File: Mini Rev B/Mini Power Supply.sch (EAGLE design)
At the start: 20 parts, among them J1 POWER_JACKPTH

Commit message: Changed the input to a JST and connected the ON LED to VCC
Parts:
- removed IADJ_SEL: (no value), pinhead:PINHD-1X2
- removed J1: POWER_JACKPTH, SparkFun-Connectors:POWER_JACKPTH
- added INPUT: M02JST-PTH-2, SparkFun-Connectors:M02JST-PTH-2
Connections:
- removed net N$4: IADJ.ADJ, IADJ_SEL.1, R3.CW, R6.1
- net GND: now also INPUT.1; no longer J1.GND, J1.GNDBREAK
- net VADJ_IN: now also IADJ.ADJ, R3.CW, R6.1; no longer IADJ_SEL.2
- net VCC: now also INPUT.2, ON.A; no longer J1.PWR
- net VOUT: no longer ON.A
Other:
- note removed: "Change the input to a JST"
- note removed: "This should be connected to VCC"
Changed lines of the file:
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@@
 <part name="R5" library="rcl" deviceset="R-EU_" device="R0805" value="100Ω"/>
 <part name="R6" library="rcl" deviceset="R-EU_" device="R0805" value="100Ω"/>
-<part name="IADJ_SEL" library="pinhead" deviceset="PINHD-1X2" device=""/>
 <part name="ON" library="led" deviceset="LED" device="CHIPLED_1206"/>
 <part name="R7" library="rcl" deviceset="R-EU_" device="R0805" value="1kΩ"/>
 <part name="GND4" library="supply1" deviceset="GND" device=""/>
 <part name="I_PRB" library="pinhead" deviceset="PINHD-1X2" device=""/>
-<part name="J1" library="SparkFun-Connectors" deviceset="POWER_JACK" device="PTH"/>
 <part name="GND6" library="supply1" deviceset="GND" device=""/>
 <part name="P+1" library="supply1" deviceset="VCC" device=""/>
 <part name="OUTPUT" library="SparkFun-Connectors" deviceset="M02" device="JST-PTH-2"/>
 <part name="SUPPLY10" library="supply2" deviceset="GND" device=""/>
+<part name="INPUT" library="SparkFun-Connectors" deviceset="M02" device="JST-PTH-2"/>
+<part name="P+3" library="supply1" deviceset="VCC" device=""/>
 </parts>
 <sheets>
 <sheet>
 <plain>
-<text x="-5.08" y="45.72" size="1.778" layer="91">Change the input
-to a JST</text>
-<text x="121.92" y="66.04" size="1.778" layer="91">This should be
-connected to VCC</text>
 <text x="76.2" y="88.9" size="1.778" layer="91">Add a current limiting
 indicator if possible</text>
@@
 <instance part="R5" gate="G$1" x="124.46" y="101.6" rot="R180"/>
 <instance part="R6" gate="G$1" x="137.16" y="101.6" rot="R180"/>
-<instance part="IADJ_SEL" gate="G$1" x="162.56" y="109.22"/>
 <instance part="ON" gate="G$1" x="134.62" y="50.8"/>
 <instance part="R7" gate="G$1" x="134.62" y="35.56" rot="R90"/>
 <instance part="GND4" gate="1" x="134.62" y="20.32"/>
 <instance part="I_PRB" gate="G$1" x="167.64" y="50.8"/>
-<instance part="J1" gate="G$1" x="12.7" y="27.94"/>
 <instance part="GND6" gate="1" x="20.32" y="17.78"/>
-<instance part="P+1" gate="VCC" x="25.4" y="50.8"/>
+<instance part="P+1" gate="VCC" x="20.32" y="50.8"/>
 <instance part="OUTPUT" gate="G$1" x="172.72" y="38.1" rot="R180"/>
 <instance part="SUPPLY10" gate="GND" x="162.56" y="25.4"/>
+<instance part="INPUT" gate="G$1" x="7.62" y="33.02"/>
+<instance part="P+3" gate="VCC" x="134.62" y="63.5"/>
 </instances>
 <busses>
@@
 </segment>
 <segment>
-<pinref part="ON" gate="G$1" pin="A"/>
-<wire x1="134.62" y1="53.34" x2="134.62" y2="60.96" width="0.1524" layer="91"/>
-<label x="132.08" y="60.96" size="1.778" layer="95"/>
-</segment>
-<segment>
 <pinref part="I_PRB" gate="G$1" pin="1"/>
 <wire x1="165.1" y1="53.34" x2="157.48" y2="53.34" width="0.1524" layer="91"/>
@@
 </segment>
 <segment>
-<pinref part="J1" gate="G$1" pin="PWR"/>
-<wire x1="15.24" y1="35.56" x2="25.4" y2="35.56" width="0.1524" layer="91"/>
+<wire x1="15.24" y1="35.56" x2="20.32" y2="35.56" width="0.1524" layer="91"/>
 <pinref part="P+1" gate="VCC" pin="VCC"/>
-<wire x1="25.4" y1="35.56" x2="25.4" y2="48.26" width="0.1524" layer="91"/>
+<wire x1="20.32" y1="35.56" x2="20.32" y2="48.26" width="0.1524" layer="91"/>
+<pinref part="INPUT" gate="G$1" pin="2"/>
+</segment>
+<segment>
+<pinref part="ON" gate="G$1" pin="A"/>
+<wire x1="134.62" y1="53.34" x2="134.62" y2="60.96" width="0.1524" layer="91"/>
+<pinref part="P+3" gate="VCC" pin="VCC"/>
 </segment>
 </net>
@@
 </segment>
 <segment>
-<pinref part="J1" gate="G$1" pin="GNDBREAK"/>
 <wire x1="15.24" y1="33.02" x2="20.32" y2="33.02" width="0.1524" layer="91"/>
-<wire x1="20.32" y1="33.02" x2="20.32" y2="30.48" width="0.1524" layer="91"/>
-<junction x="20.32" y="30.48"/>
-<wire x1="20.32" y1="30.48" x2="20.32" y2="20.32" width="0.1524" layer="91"/>
-<pinref part="J1" gate="G$1" pin="GND"/>
-<wire x1="15.24" y1="30.48" x2="20.32" y2="30.48" width="0.1524" layer="91"/>
+<wire x1="20.32" y1="33.02" x2="20.32" y2="20.32" width="0.1524" layer="91"/>
 <pinref part="GND6" gate="1" pin="GND"/>
+<pinref part="INPUT" gate="G$1" pin="1"/>
 </segment>
 <segment>
@@
 </segment>
 <segment>
-<pinref part="IADJ_SEL" gate="G$1" pin="2"/>
-<wire x1="160.02" y1="109.22" x2="152.4" y2="109.22" width="0.1524" layer="91"/>
-<wire x1="152.4" y1="109.22" x2="152.4" y2="88.9" width="0.1524" layer="91"/>
-<label x="147.32" y="86.36" size="1.778" layer="95"/>
+<label x="162.56" y="114.3" size="1.778" layer="95" rot="R180"/>
+<pinref part="IADJ" gate="1" pin="ADJ"/>
+<wire x1="88.9" y1="104.14" x2="88.9" y2="96.52" width="0.1524" layer="91"/>
+<pinref part="R3" gate="R?" pin="CW"/>
+<wire x1="129.54" y1="111.76" x2="147.32" y2="111.76" width="0.1524" layer="91"/>
+<pinref part="R6" gate="G$1" pin="1"/>
+<wire x1="142.24" y1="101.6" x2="147.32" y2="101.6" width="0.1524" layer="91"/>
+<wire x1="147.32" y1="101.6" x2="147.32" y2="111.76" width="0.1524" layer="91"/>
+<junction x="147.32" y="111.76"/>
+<wire x1="147.32" y1="111.76" x2="157.48" y2="111.76" width="0.1524" layer="91"/>
+<wire x1="88.9" y1="96.52" x2="147.32" y2="96.52" width="0.1524" layer="91"/>
+<wire x1="147.32" y1="96.52" x2="147.32" y2="101.6" width="0.1524" layer="91"/>
+<junction x="147.32" y="101.6"/>
 </segment>
 </net>
@@
 </segment>
 </net>
-<net name="N$4" class="0">
-<segment>
-<pinref part="IADJ" gate="1" pin="ADJ"/>
-<wire x1="88.9" y1="104.14" x2="88.9" y2="96.52" width="0.1524" layer="91"/>
-<pinref part="R3" gate="R?" pin="CW"/>
-<wire x1="129.54" y1="111.76" x2="147.32" y2="111.76" width="0.1524" layer="91"/>
-<pinref part="R6" gate="G$1" pin="1"/>
-<wire x1="142.24" y1="101.6" x2="147.32" y2="101.6" width="0.1524" layer="91"/>
-<wire x1="147.32" y1="101.6" x2="147.32" y2="111.76" width="0.1524" layer="91"/>
-<junction x="147.32" y="111.76"/>
-<wire x1="147.32" y1="111.76" x2="160.02" y2="111.76" width="0.1524" layer="91"/>
-<wire x1="88.9" y1="96.52" x2="147.32" y2="96.52" width="0.1524" layer="91"/>
-<wire x1="147.32" y1="96.52" x2="147.32" y2="101.6" width="0.1524" layer="91"/>
-<junction x="147.32" y="101.6"/>
-<pinref part="IADJ_SEL" gate="G$1" pin="1"/>
-</segment>
-</net>

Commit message: Finished most of the new revision
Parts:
- added Q1: BC817-25LT1SMD, transistor-npn:BC817-25LT1SMD
- added R8: 1kΩ, rcl:R-EU_R0805
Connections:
- new net N$4: Q1.C, R7.1
- new net N$8: Q1.B, R8.2
- net GND: now also Q1.E; no longer R7.1
- net VOUT: now also R8.1
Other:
- note added: "Add an ON/OFF switch"
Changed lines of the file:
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@@
 <part name="INPUT" library="SparkFun-Connectors" deviceset="M02" device="JST-PTH-2"/>
 <part name="P+3" library="supply1" deviceset="VCC" device=""/>
+<part name="Q1" library="transistor-npn" deviceset="BC817*" device="SMD" technology="-25LT1"/>
+<part name="R8" library="rcl" deviceset="R-EU_" device="R0805" value="1kΩ"/>
 </parts>
 <sheets>
@@
 <text x="5.08" y="81.28" size="1.778" layer="91">Add some awesome
 logos to the board</text>
+<text x="-5.08" y="91.44" size="1.778" layer="91">Add an ON/OFF
+switch</text>
 </plain>
 <instances>
@@
 <instance part="ON" gate="G$1" x="134.62" y="50.8"/>
 <instance part="R7" gate="G$1" x="134.62" y="35.56" rot="R90"/>
-<instance part="GND4" gate="1" x="134.62" y="20.32"/>
+<instance part="GND4" gate="1" x="134.62" y="7.62"/>
 <instance part="I_PRB" gate="G$1" x="167.64" y="50.8"/>
 <instance part="GND6" gate="1" x="20.32" y="17.78"/>
@@
 <instance part="INPUT" gate="G$1" x="7.62" y="33.02"/>
 <instance part="P+3" gate="VCC" x="134.62" y="63.5"/>
+<instance part="Q1" gate="G$1" x="132.08" y="20.32"/>
+<instance part="R8" gate="G$1" x="119.38" y="20.32"/>
 </instances>
 <busses>
@@
 <label x="154.94" y="66.04" size="1.778" layer="95"/>
 </segment>
+<segment>
+<pinref part="R8" gate="G$1" pin="1"/>
+<wire x1="114.3" y1="20.32" x2="109.22" y2="20.32" width="0.1524" layer="91"/>
+<wire x1="109.22" y1="20.32" x2="109.22" y2="30.48" width="0.1524" layer="91"/>
+<label x="111.76" y="33.02" size="1.778" layer="95" rot="R180"/>
+</segment>
 </net>
 <net name="N$3" class="0">
@@
 </segment>
 <segment>
-<pinref part="R7" gate="G$1" pin="1"/>
-<wire x1="134.62" y1="30.48" x2="134.62" y2="22.86" width="0.1524" layer="91"/>
-<pinref part="GND4" gate="1" pin="GND"/>
-</segment>
-<segment>
 <wire x1="15.24" y1="33.02" x2="20.32" y2="33.02" width="0.1524" layer="91"/>
 <wire x1="20.32" y1="33.02" x2="20.32" y2="20.32" width="0.1524" layer="91"/>
@@
 <wire x1="162.56" y1="38.1" x2="162.56" y2="27.94" width="0.1524" layer="91"/>
 <pinref part="SUPPLY10" gate="GND" pin="GND"/>
+</segment>
+<segment>
+<pinref part="Q1" gate="G$1" pin="E"/>
+<pinref part="GND4" gate="1" pin="GND"/>
+<wire x1="134.62" y1="15.24" x2="134.62" y2="10.16" width="0.1524" layer="91"/>
 </segment>
 </net>
@@
 </segment>
 </net>
+<net name="N$4" class="0">
+<segment>
+<pinref part="Q1" gate="G$1" pin="C"/>
+<pinref part="R7" gate="G$1" pin="1"/>
+<wire x1="134.62" y1="25.4" x2="134.62" y2="30.48" width="0.1524" layer="91"/>
+</segment>
+</net>
+<net name="N$8" class="0">
+<segment>
+<pinref part="Q1" gate="G$1" pin="B"/>
+<wire x1="129.54" y1="20.32" x2="124.46" y2="20.32" width="0.1524" layer="91"/>
+<pinref part="R8" gate="G$1" pin="2"/>
+</segment>
+</net>

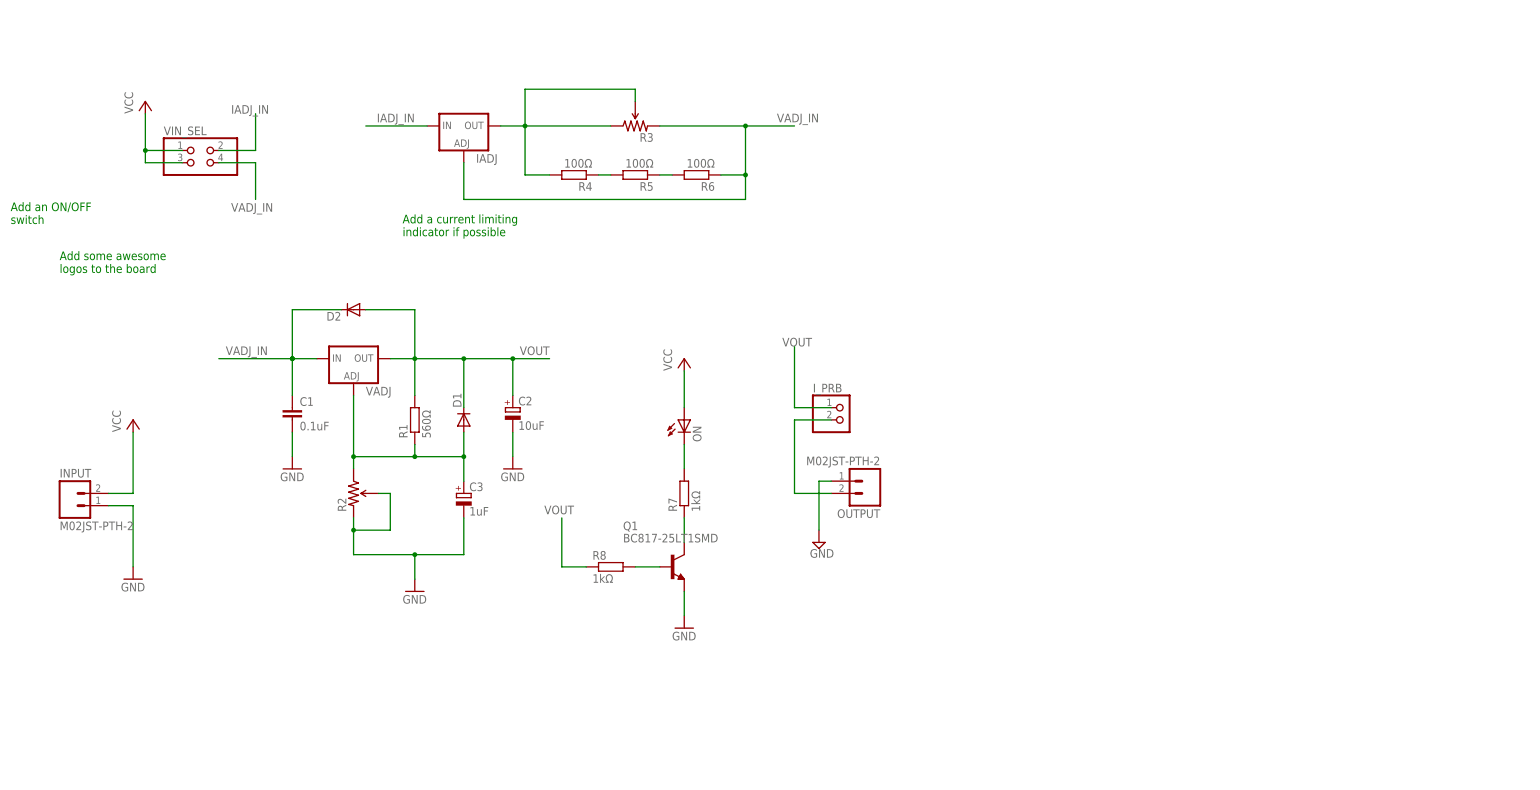
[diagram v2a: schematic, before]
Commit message: Started working on the negative rail for the mini Rev B
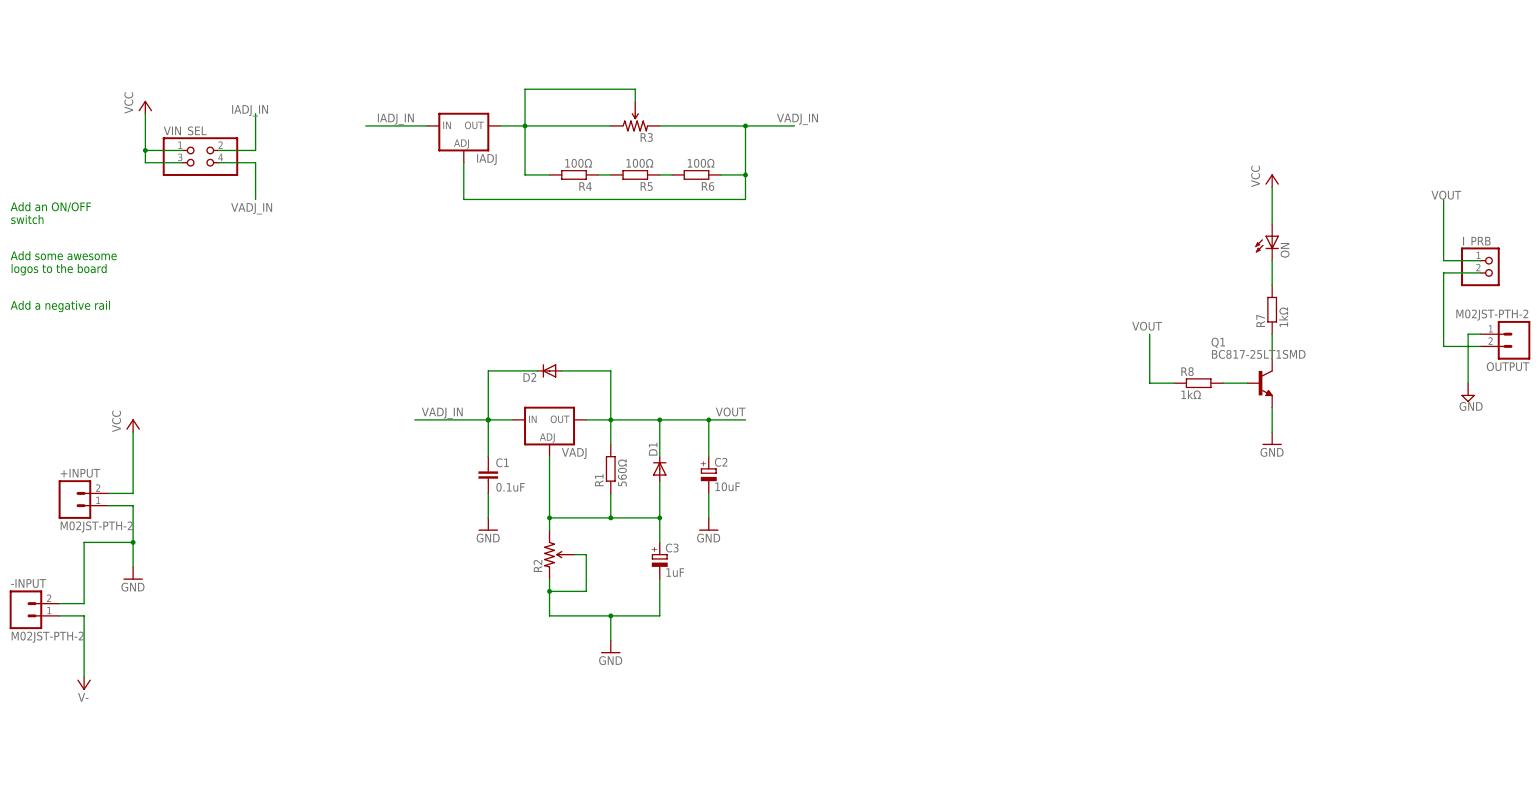
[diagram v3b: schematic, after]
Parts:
- added -INPUT: M02JST-PTH-2, SparkFun-Connectors:M02JST-PTH-2
- renumbered INPUT to +INPUT
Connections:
- new net V-: -INPUT.1
- net GND: now also -INPUT.2
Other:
- note added: "Add a negative rail"
- note removed: "Add a current limiting indicator if possible"
- moved on the sheet: C1, C2, C3, D1, D2, I_PRB, ON, OUTPUT, Q1, R1, R2, R7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

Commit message: Finished the negative rail
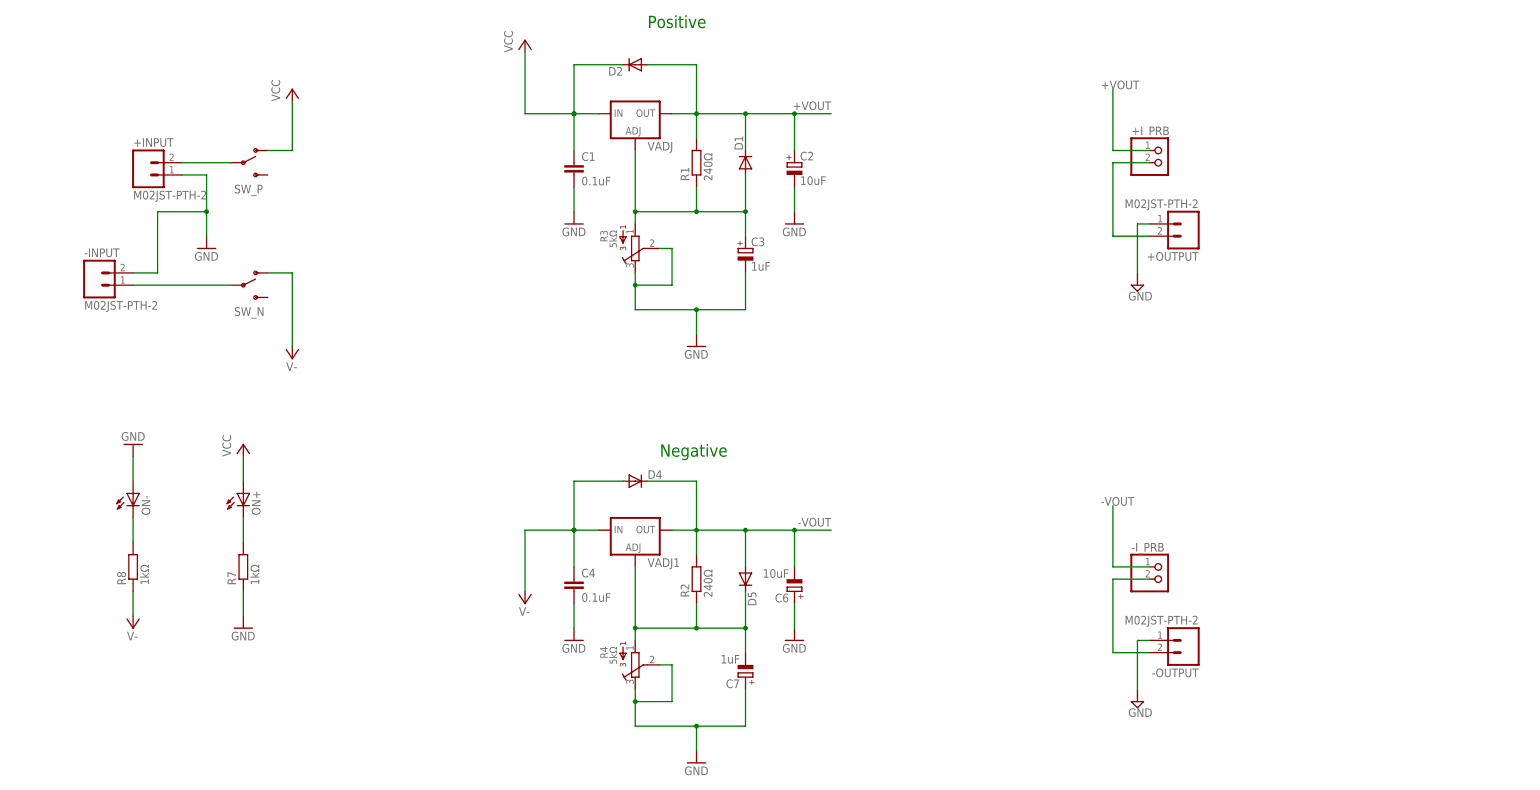
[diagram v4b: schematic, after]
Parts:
- removed IADJ: (no value), v-reg:LM317TS
- removed I_PRB: (no value), pinhead:PINHD-1X2
- removed ON: (no value), led:LEDCHIPLED_1206
- removed OUTPUT: M02JST-PTH-2, SparkFun-Connectors:M02JST-PTH-2
- removed Q1: BC817-25LT1SMD, transistor-npn:BC817-25LT1SMD
- removed R5, R6: 100Ω, rcl:R-EU_R0805
- removed VIN_SEL: (no value), pinhead:PINHD-2X2
- added +I_PRB, -I_PRB: (no value), pinhead:PINHD-1X2
- added +OUTPUT, -OUTPUT: M02JST-PTH-2, SparkFun-Connectors:M02JST-PTH-2
- added C4: 0.1uF, rcl:C-EUC0805
- added C6: 10uF, rcl:CPOL-EUE2.5-6
- added C7: 1uF, rcl:CPOL-EUE2.5-6
- added D4, D5: (no value), diode:DIODE-SOD323-W
- added ON+, ON-: (no value), led:LEDCHIPLED_1206
- added SW_N, SW_P: (no value), SparkFun-Electromechanical:SWITCH-SPDTPTH_LOCK
- added VADJ1: (no value), v-reg:LM317TS
- R1: value 560Ω -> 240Ω
- R2: value TRIMPOT-PTH-KNOB -> 240Ω; device SparkFun-Electromechanical:TRIMPOT-PTH-KNOB -> rcl:R-EU_R0805
- R3: value TRIMPOT-PTH-KNOB -> 5kΩ; device SparkFun-Electromechanical:TRIMPOT-PTH-KNOB -> bourns:3386-W
- R4: value 100Ω -> 5kΩ; device rcl:R-EU_R0805 -> bourns:3386-W
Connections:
- removed net IADJ_IN: IADJ.IN, VIN_SEL.2
- removed net N$8: Q1.B, R8.2
- removed net VADJ_IN: C1.1, D2.C, IADJ.ADJ, R3.CW, R6.1, VADJ.IN, VIN_SEL.4
- removed net VOUT: C2.+, D1.C, D2.A, I_PRB.1, R1.2, R8.1, VADJ.OUT
- new net +VOUT: +I_PRB.1, C2.+, D1.C, D2.A, R1.2, VADJ.OUT
- new net -VOUT: -I_PRB.1, C6.-, D4.C, D5.A, R2.2, VADJ1.OUT
- new net N$10: -I_PRB.2, -OUTPUT.2
- net GND: now also +OUTPUT.1, -OUTPUT.1, C4.2, C6.+, C7.+, ON-.A, R3.2, R3.3, R4.2, R4.3, R7.1; no longer OUTPUT.1, Q1.E, R2.CW, R2.WIPER
- net N$1: now also C7.-, D5.C, R2.1, R4.1, VADJ1.ADJ; no longer IADJ.OUT, R3.CCW, R3.WIPER, R4.2
- net N$2: now also +INPUT.2, SW_P.P; no longer R4.1, R5.2
- net N$3: now also R3.1; no longer R2.CCW
- net N$4: now also ON-.C, R8.2; no longer Q1.C, R7.1
- net N$5: now also -INPUT.1, SW_N.P; no longer R5.1, R6.2
- net N$6: now also ON+.C; no longer ON.C
- net N$7: now also +I_PRB.2, +OUTPUT.2; no longer I_PRB.2, OUTPUT.2
- net V-: now also C4.1, D4.A, R8.1, SW_N.O, VADJ1.IN; no longer -INPUT.1
- net VCC: now also C1.1, D2.C, ON+.A, SW_P.O, VADJ.IN; no longer +INPUT.2, ON.A, VIN_SEL.1, VIN_SEL.3
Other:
- note added: "Negative"
- note added: "Positive"
- note removed: "Add a negative rail"
- note removed: "Add an ON/OFF switch"
- note removed: "Add some awesome logos to the board"
- moved on the sheet: +INPUT, -INPUT, C1, C2, C3, D1, D2, R1, R7, R8, VADJ

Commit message: Redid the Mini Rev B
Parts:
- removed +OUTPUT, -OUTPUT: M02JST-PTH-2, SparkFun-Connectors:M02JST-PTH-2
- removed R7, R8: 1kΩ, rcl:R-EU_R0805
- removed SW_N, SW_P: (no value), SparkFun-Electromechanical:SWITCH-SPDTPTH_LOCK
- added +OUTPUT1, -OUTPUT1: M02JST-PTH-2, SparkFun-Connectors:M02JST-PTH-2
- added JP1, JP2: (no value), pinhead:PINHD-1X2
- added R6, R9: 1kΩ, resistor:R-EU_0207/10
- added S1: (no value), switch-dil:DIP02YL
- C1, C4: value 0.1uF -> 2.2uF; device rcl:C-EUC0805 -> rcl:CPOL-EUE2.5-6
- D1, D2, D4, D5: value (none) -> 1N4148DO35-7; device diode:DIODE-SOD323-W -> diode:1N4148DO35-7
- ON+, ON-: device led:LEDCHIPLED_1206 -> led:LEDSQR2X5
- R1, R2: device rcl:R-EU_R0805 -> resistor:R-EU_0207/10
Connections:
- net GND: now also +OUTPUT1.1, -OUTPUT1.1, C1.-, C4.+, JP1.1, JP2.1, R6.1; no longer +OUTPUT.1, -OUTPUT.1, C1.2, C4.2, R7.1
- net N$10: now also -OUTPUT1.2, JP1.2; no longer -OUTPUT.2
- net N$2: now also S1.1; no longer SW_P.P
- net N$4: now also R9.2; no longer R8.2
- net N$5: now also S1.2; no longer SW_N.P
- net N$6: now also R6.2; no longer R7.2
- net N$7: now also +OUTPUT1.2, JP2.2; no longer +OUTPUT.2
- net V-: now also C4.-, R9.1, S1.3; no longer C4.1, R8.1, SW_N.O
- net VCC: now also C1.+, S1.4; no longer C1.1, SW_P.O
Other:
- moved on the sheet: -INPUT

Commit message: Finished the layout for Mini Rev B
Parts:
- removed C7: 1uF, rcl:CPOL-EUE2.5-6
- removed VADJ, VADJ1: (no value), v-reg:LM317TS
- added C5: 10uF, rcl:CPOL-EUE2.5-6
- added VADJ+, VADJ-: (no value), v-reg:LM317L
- C6: value 10uF -> 1uF
- R3, R4: device bourns:3386-W -> bourns:3386-U
- renumbered +OUTPUT1 to +OUTPUT, -OUTPUT1 to -OUTPUT, D5 to D3, JP1 to VOUT-, JP2 to VOUT+
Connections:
- net +VOUT: now also VADJ+.OUT; no longer VADJ.OUT
- net -VOUT: now also C5.-, VADJ-.OUT; no longer C6.-, VADJ1.OUT
- net GND: now also C5.+; no longer C7.+
- net N$1: now also C6.-, VADJ-.ADJ; no longer C7.-, VADJ1.ADJ
- net N$3: now also VADJ+.ADJ; no longer VADJ.ADJ
- net V-: now also VADJ-.IN; no longer VADJ1.IN
- net VCC: now also VADJ+.IN; no longer VADJ.IN
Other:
- moved on the sheet: C6
